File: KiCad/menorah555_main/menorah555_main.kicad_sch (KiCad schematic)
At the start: 94 parts, among them J1 USB_B_Micro, J2 Jack5.5x2.1, Q1 MMBT3904, Q10 MJD31, Q2 MMBT3904, Q3 MMBT3904, Q4 MMBT3904, Q5 MMBT3904, Q6 MMBT3904, Q7 MMBT3904, Q8 MMBT3904, Q9 MMBT3904, SW1 SW_Reed, SW2 SW_Reed, SW3 SW_Reed, SW4 SW_Reed, SW5 SW_Reed, SW6 SW_Reed, SW7 SW_Reed, SW8 SW_Reed, SW9 SW_DPDT, U1 TLC555, U2 TLC555, U3 TLC555, U4 TLC555, U5 TLC555, U6 TLC555, U7 TLC555, U8 TLC555, U9 TLC555

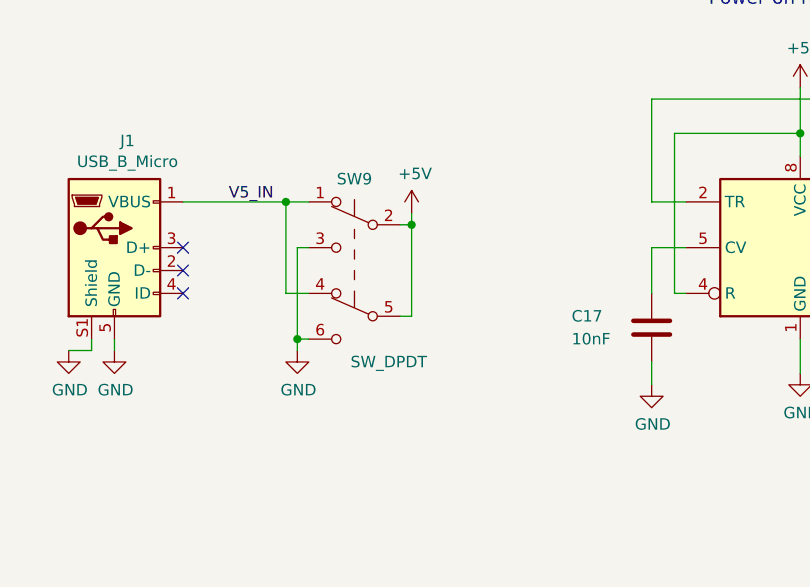
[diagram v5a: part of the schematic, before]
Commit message: Updated slide switch to ground the case
The Nidec slide switch case had pins named 'M' that were not on the
schematic, so they did not get connected on the PCB. Now those pins have
been added to the symbol and connected to ground.
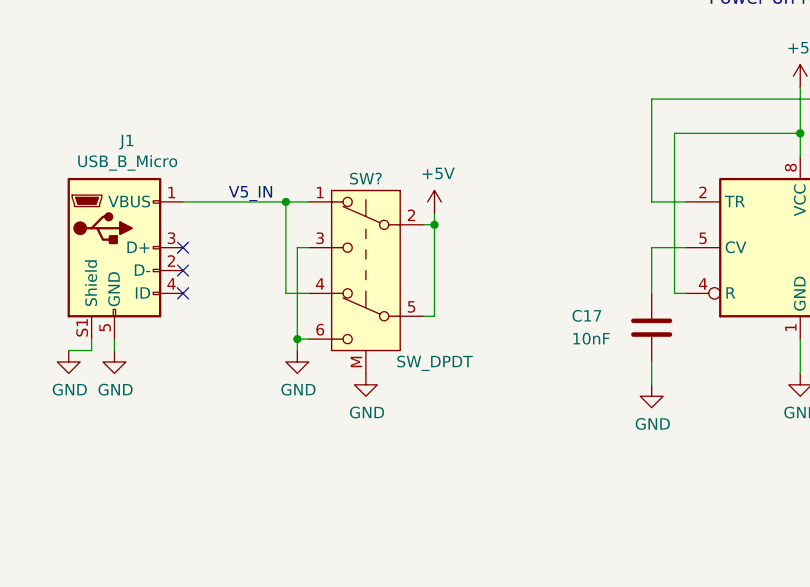
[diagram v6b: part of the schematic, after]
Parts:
- removed SW9: SW_DPDT, 0_my_footprints:SW_Nidec_MFS201N-9-Z_DPDT_Straight, symbol Switch:SW_Push_DPDT
- added SW?: SW_DPDT, 0_my_footprints:SW_Nidec_MFS201N-9-Z_DPDT_Straight, symbol 0_project_symbol_library:SW_DPDT_Nidec_MFS201N-9-Z
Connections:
- net +5V: now also SW?.2 (B), SW?.5 (B)
- net GND: now also SW?.3 (C), SW?.6 (C), SW?.M
- net V5_IN: now also SW?.1 (A), SW?.4 (A)
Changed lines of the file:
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@@
   (junction (at 219.71 119.38) (diameter 0) (color 0 0 0 0)
   )
-  (junction (at 96.52 209.55) (diameter 0) (color 0 0 0 0)
+  (junction (at 99.06 209.55) (diameter 0) (color 0 0 0 0)
   )
   (junction (at 334.01 107.95) (diameter 0) (color 0 0 0 0)
@@
     (stroke (width 0) (type default) (color 0 0 0 0))
   )
-  (wire (pts (xy 95.25 209.55) (xy 96.52 209.55))
+  (wire (pts (xy 97.79 209.55) (xy 99.06 209.55))
     (stroke (width 0) (type default) (color 0 0 0 0))
   )
@@
     (stroke (width 0) (type default) (color 0 0 0 0))
   )
-  (wire (pts (xy 96.52 208.28) (xy 96.52 209.55))
+  (wire (pts (xy 99.06 208.28) (xy 99.06 209.55))
     (stroke (width 0) (type default) (color 0 0 0 0))
   )
@@
     (stroke (width 0) (type default) (color 0 0 0 0))
   )
-  (wire (pts (xy 96.52 209.55) (xy 96.52 219.71))
+  (wire (pts (xy 99.06 209.55) (xy 99.06 219.71))
     (stroke (width 0) (type default) (color 0 0 0 0))
   )
@@
     (stroke (width 0) (type default) (color 0 0 0 0))
   )
-  (wire (pts (xy 96.52 219.71) (xy 95.25 219.71))
+  (wire (pts (xy 99.06 219.71) (xy 97.79 219.71))
     (stroke (width 0) (type default) (color 0 0 0 0))
   )
@@
     (pin "3")
   )
-  (symbol (lib_id "Switch:SW_Push_DPDT") (at 90.17 214.63 0) (mirror y) (unit 1)
-    (in_bom yes) (on_board yes)
-    (property "Reference" "SW9" (id 0) (at 90.17 204.47 0))
-    (property "Value" "SW_DPDT" (id 1) (at 93.98 224.79 0))
-    (property "Footprint" "0_my_footprints:SW_Nidec_MFS201N-9-Z_DPDT_Straight" (id 2) (at 90.17 209.55 0)
-      (effects (font (size 1.27 1.27)) hide)
-    )
-    (property "Datasheet" "~" (id 3) (at 90.17 209.55 0)
-      (effects (font (size 1.27 1.27)) hide)
-    )
-    (property "Source" "Mouser 229-MFS201N-9-Z" (id 4) (at 90.17 214.63 0)
-      (effects (font (size 1.27 1.27)) hide)
-    )
-    (pin "1")
-    (pin "2")
-    (pin "3")
-    (pin "4")
-    (pin "5")
-    (pin "6")
-  )
   (symbol (lib_id "0_project_symbol_library:Amphenol_10118194-0001LF_USB_B_Micro") (at 63.5 212.09 0) (unit 1)
     (in_bom yes) (on_board yes)
@@
     (pin "1")
   )
-  (symbol (lib_id "power:+5V") (at 96.52 208.28 0) (unit 1)
+  (symbol (lib_id "power:+5V") (at 99.06 208.28 0) (unit 1)
     (in_bom yes) (on_board yes)
-    (property "Reference" "#PWR09" (id 0) (at 96.52 212.09 0)
+    (property "Reference" "#PWR09" (id 0) (at 99.06 212.09 0)
       (effects (font (size 1.27 1.27)) hide)
     )
-    (property "Value" "+5V" (id 1) (at 96.901 203.8858 0))
-    (property "Footprint" "" (id 2) (at 96.52 208.28 0)
+    (property "Value" "+5V" (id 1) (at 99.441 203.8858 0))
+    (property "Footprint" "" (id 2) (at 99.06 208.28 0)
       (effects (font (size 1.27 1.27)) hide)
     )
-    (property "Datasheet" "" (id 3) (at 96.52 208.28 0)
+    (property "Datasheet" "" (id 3) (at 99.06 208.28 0)
       (effects (font (size 1.27 1.27)) hide)
     )
@@
     (pin "1")
   )
+  (symbol (lib_id "power:GND") (at 91.44 226.06 0) (unit 1)
+    (in_bom yes) (on_board yes)
+    (property "Reference" "#PWR?" (id 0) (at 91.44 232.41 0)
+      (effects (font (size 1.27 1.27)) hide)
+    )
+    (property "Value" "GND" (id 1) (at 91.567 230.4542 0))
+    (property "Footprint" "" (id 2) (at 91.44 226.06 0)
+      (effects (font (size 1.27 1.27)) hide)
+    )
+    (property "Datasheet" "" (id 3) (at 91.44 226.06 0)
+      (effects (font (size 1.27 1.27)) hide)
+    )
+    (pin "1")
+  )
+  (symbol (lib_id "0_project_symbol_library:SW_DPDT_Nidec_MFS201N-9-Z") (at 91.44 214.63 0) (mirror y) (unit 1)
+    (in_bom yes) (on_board yes)
+    (property "Reference" "SW?" (id 0) (at 91.44 204.47 0))
+    (property "Value" "SW_DPDT" (id 1) (at 99.06 224.79 0))
+    (property "Footprint" "0_my_footprints:SW_Nidec_MFS201N-9-Z_DPDT_Straight" (id 2) (at 91.44 209.55 0)
+      (effects (font (size 1.27 1.27)) hide)
+    )
+    (property "Datasheet" "~" (id 3) (at 91.44 209.55 0)
+      (effects (font (size 1.27 1.27)) hide)
+    )
+    (property "Source" "Mouser 229-MFS201N-9-Z" (id 4) (at 91.44 214.63 0)
+      (effects (font (size 1.27 1.27)) hide)
+    )
+    (pin "1")
+    (pin "2")
+    (pin "3")
+    (pin "4")
+    (pin "5")
+    (pin "6")
+    (pin "M")
+  )
   (symbol (lib_id "Diode:BAV99") (at 356.87 107.95 270) (unit 1)
     (in_bom yes) (on_board yes)
@@
       (reference "#PWR0102") (unit 1) (value "+5V") (footprint "")
     )
+    (path "/2b04795e-1027-4310-a956-b1633bcb750a"
+      (reference "#PWR?") (unit 1) (value "GND") (footprint "")
+    )
     (path "/00000000-0000-0000-0000-000061aca084"
       (reference "C1") (unit 1) (value "10nF") (footprint "Capacitor_SMD:C_0805_2012Metric")
@@
       (reference "SW8") (unit 1) (value "SW_Reed") (footprint "0_my_footprints:SW_SPST_REED_59170-1-S-00-D")
     )
-    (path "/00000000-0000-0000-0000-000061bac8aa"
-      (reference "SW9") (unit 1) (value "SW_DPDT") (footprint "0_my_footprints:SW_Nidec_MFS201N-9-Z_DPDT_Straight")
+    (path "/95629a0f-30f0-46d6-99ad-b005fd9dcc25"
+      (reference "SW?") (unit 1) (value "SW_DPDT") (footprint "0_my_footprints:SW_Nidec_MFS201N-9-Z_DPDT_Straight")
     )
     (path "/00000000-0000-0000-0000-000061aa0766"

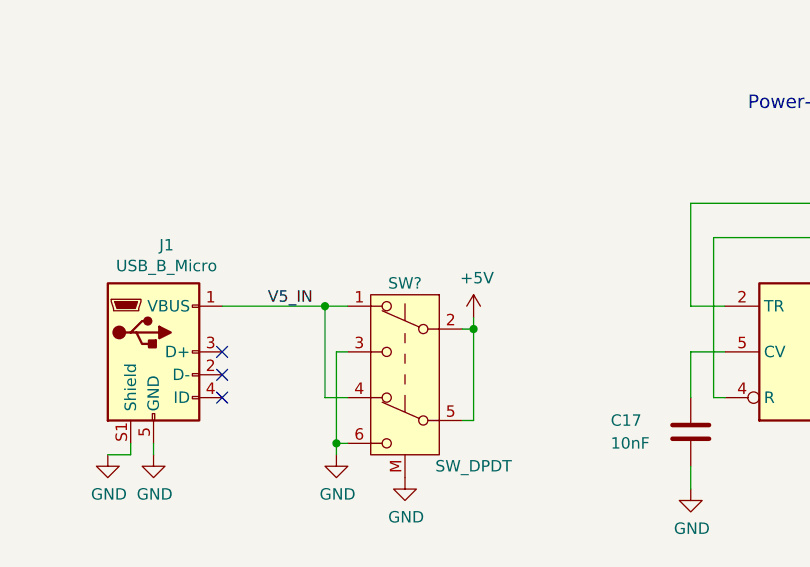
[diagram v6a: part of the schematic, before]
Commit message: Added silkscreen 2mm stripe at edge
For aesthetic reasons, a 2mm silkscreen strip was added around the board
on top and bottom. Gerbers were also generated
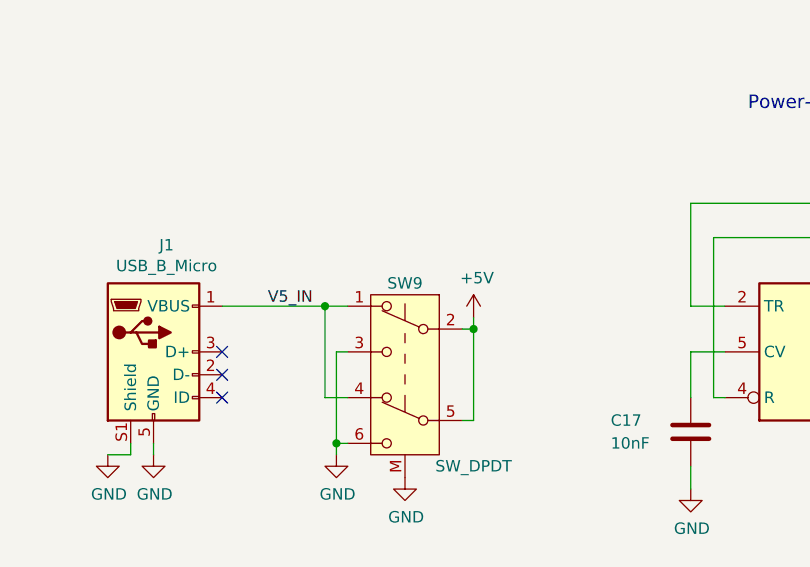
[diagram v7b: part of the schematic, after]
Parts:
- gave numbers to parts that had none: 1
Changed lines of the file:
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@@
   (symbol (lib_id "power:GND") (at 91.44 226.06 0) (unit 1)
     (in_bom yes) (on_board yes)
-    (property "Reference" "#PWR?" (id 0) (at 91.44 232.41 0)
+    (property "Reference" "#PWR0103" (id 0) (at 91.44 232.41 0)
       (effects (font (size 1.27 1.27)) hide)
     )
@@
   (symbol (lib_id "0_project_symbol_library:SW_DPDT_Nidec_MFS201N-9-Z") (at 91.44 214.63 0) (mirror y) (unit 1)
     (in_bom yes) (on_board yes)
-    (property "Reference" "SW?" (id 0) (at 91.44 204.47 0))
+    (property "Reference" "SW9" (id 0) (at 91.44 204.47 0))
     (property "Value" "SW_DPDT" (id 1) (at 99.06 224.79 0))
     (property "Footprint" "0_my_footprints:SW_Nidec_MFS201N-9-Z_DPDT_Straight" (id 2) (at 91.44 209.55 0)
@@
     )
     (path "/2b04795e-1027-4310-a956-b1633bcb750a"
-      (reference "#PWR?") (unit 1) (value "GND") (footprint "")
+      (reference "#PWR0103") (unit 1) (value "GND") (footprint "")
     )
     (path "/00000000-0000-0000-0000-000061aca084"
@@
     )
     (path "/95629a0f-30f0-46d6-99ad-b005fd9dcc25"
-      (reference "SW?") (unit 1) (value "SW_DPDT") (footprint "0_my_footprints:SW_Nidec_MFS201N-9-Z_DPDT_Straight")
+      (reference "SW9") (unit 1) (value "SW_DPDT") (footprint "0_my_footprints:SW_Nidec_MFS201N-9-Z_DPDT_Straight")
     )
     (path "/00000000-0000-0000-0000-000061aa0766"
